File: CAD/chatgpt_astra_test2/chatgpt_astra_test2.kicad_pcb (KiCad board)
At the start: 4 copper layers, 100 x 80 mm, 97 parts, among them J1 18-30 V DC, J2 CURRENT INPUT, J3 CURRENT OUTPUT, J4 USB-C, J5 UART / 3.3 V ONLY, Q1 2N7002, Q2 2N7002, Q3 IRF9540NPBF, Q4 MMBT3906, SW1 RESET, SW2 BOOT, U1 TPS26600PWPR, U10 ADS1115IDGSR, U11 DAC80501ZDGSR, U12 XTR111AIDGQR, U2 LMR36510ADDAR, U3 LT3092EST#PBF, U4 ESP32-S3-WROOM-1-N8, U5 TPS3839G33DBZR, U6 USBLC6-2SC6, U7 LT3092EST#PBF, U8 LM4040AIM3-3.0, U9 TMUX1511PWR

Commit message: Start buck converter and DAC PCB routing
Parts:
- moved C5 4.39 mm to (61.5, 84.4), turned to 90 degrees
- moved C6 4.02 mm to (72.5, 83.7), turned to 90 degrees
- moved C4 2.50 mm to (58.5, 82.0)
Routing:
- net V3V3: track 0.00 -> 23.0 mm
- net /05 / PRECISION CURRENT OUTPUT/DAC_FILTER: track 0.00 -> 10.6 mm
- net /05 / PRECISION CURRENT OUTPUT/DAC_RAW: track 0.00 -> 10.0 mm
- net /02 / POWER AND SENSOR SUPPLY/BUCK_VCC: track 0.00 -> 10.0 mm
- net V24_PROT: track 0.00 -> 8.63 mm
- net GND: track 0.00 -> 7.65 mm
- net /02 / POWER AND SENSOR SUPPLY/BUCK_SW: track 0.00 -> 7.10 mm
- net /02 / POWER AND SENSOR SUPPLY/BUCK_FB: track 0.00 -> 6.00 mm
- net /05 / PRECISION CURRENT OUTPUT/DAC_REF: track 0.00 -> 3.19 mm
- net /02 / POWER AND SENSOR SUPPLY/BUCK_BOOT: track 0.00 -> 2.76 mm
- net /05 / PRECISION CURRENT OUTPUT/XTR_REG: track 0.00 -> 0.50 mm
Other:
- board text added: "REV A - ROUTING DRAFT"
- board text removed: "REV A - PLACEMENT"

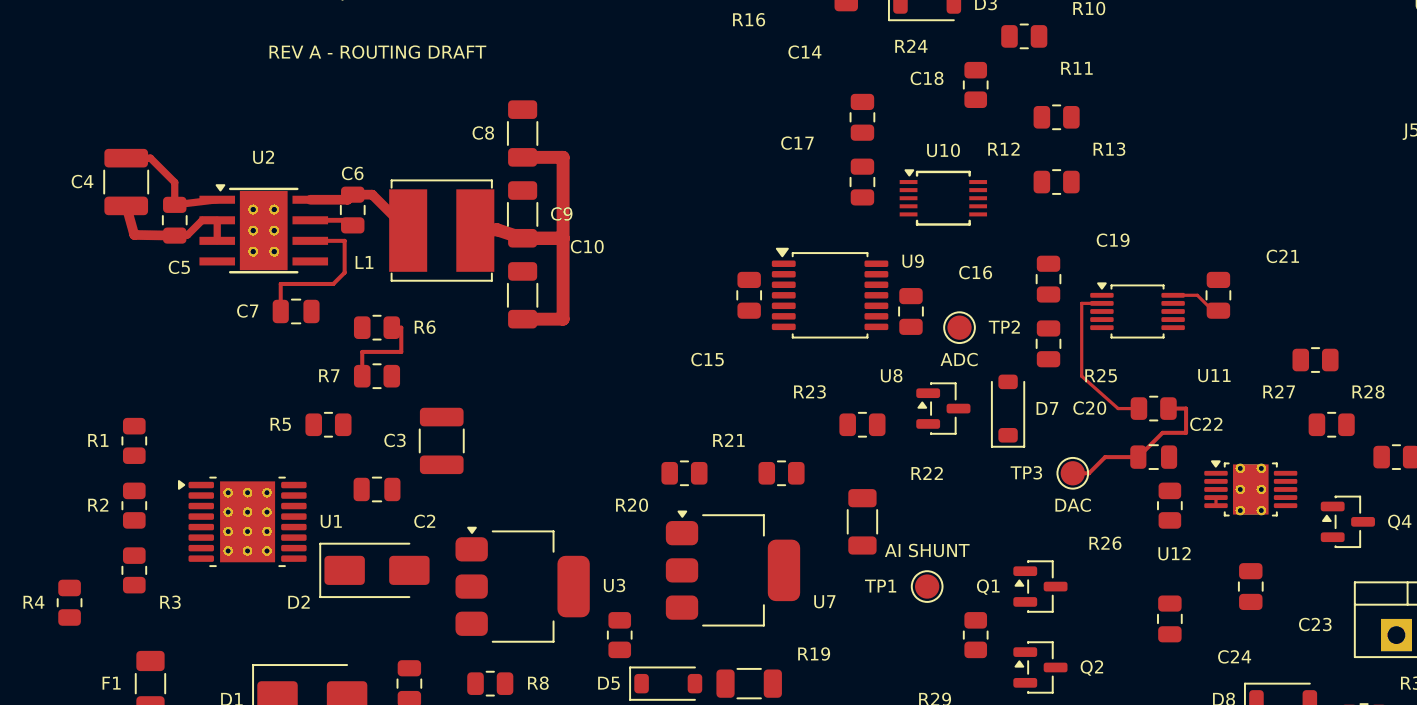
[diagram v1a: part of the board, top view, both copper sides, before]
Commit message: Route buck feedback and analog sense connections
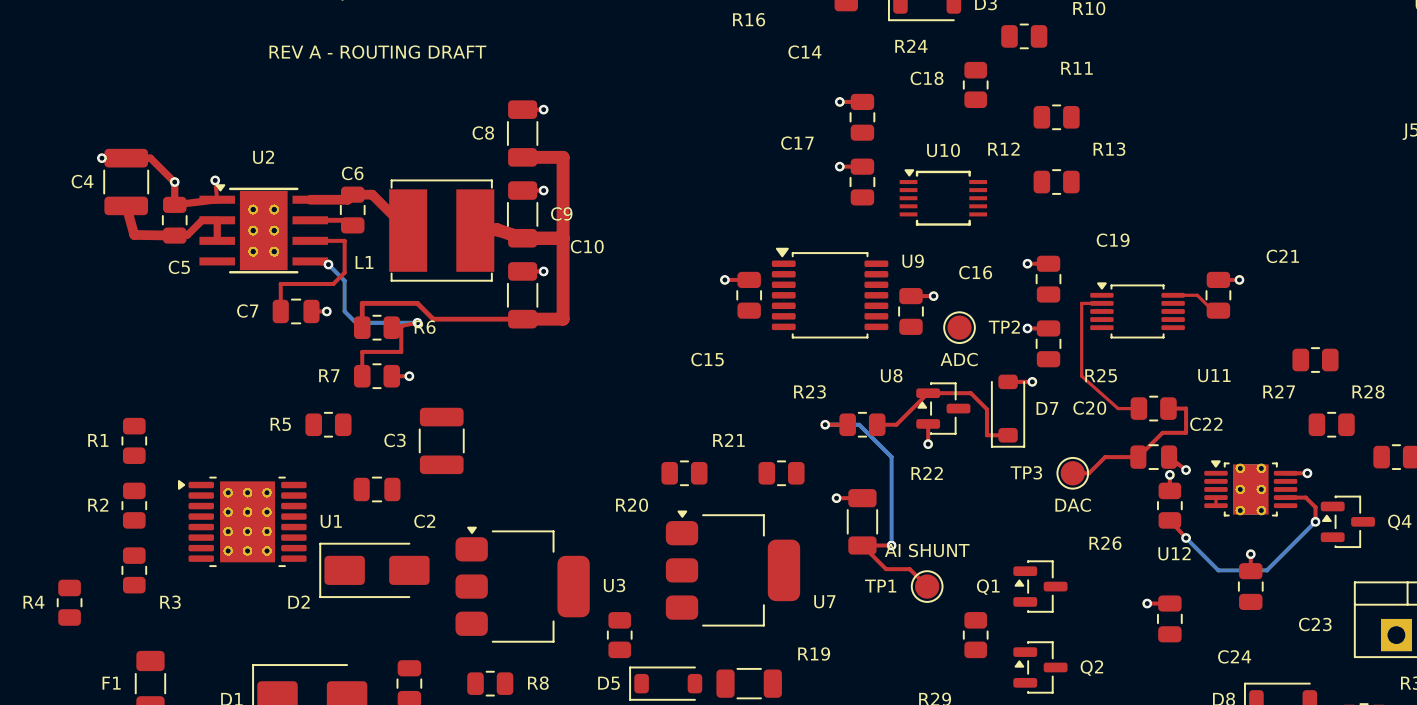
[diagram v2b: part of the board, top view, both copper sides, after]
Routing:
- net GND: track 7.65 -> 37.8 mm, vias 0 -> 23
- net /04 / PROTECTED CURRENT INPUT/AI_SHUNT: track 0.00 -> 18.6 mm, vias 0 -> 2
- net /05 / PRECISION CURRENT OUTPUT/XTR_SET: track 0.00 -> 14.5 mm, vias 0 -> 2
- net V3V3: track 23.0 -> 34.8 mm
- net /04 / PROTECTED CURRENT INPUT/AI_CLAMP: track 0.00 -> 10.9 mm
- net /02 / POWER AND SENSOR SUPPLY/BUCK_FB: track 6.00 -> 16.9 mm, vias 0 -> 2
